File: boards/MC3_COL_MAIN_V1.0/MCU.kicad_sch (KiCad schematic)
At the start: 19 parts, among them J2 SWD, SW1 SKRKAEE020, U2 STM32F411RET6, Y1 8MHz

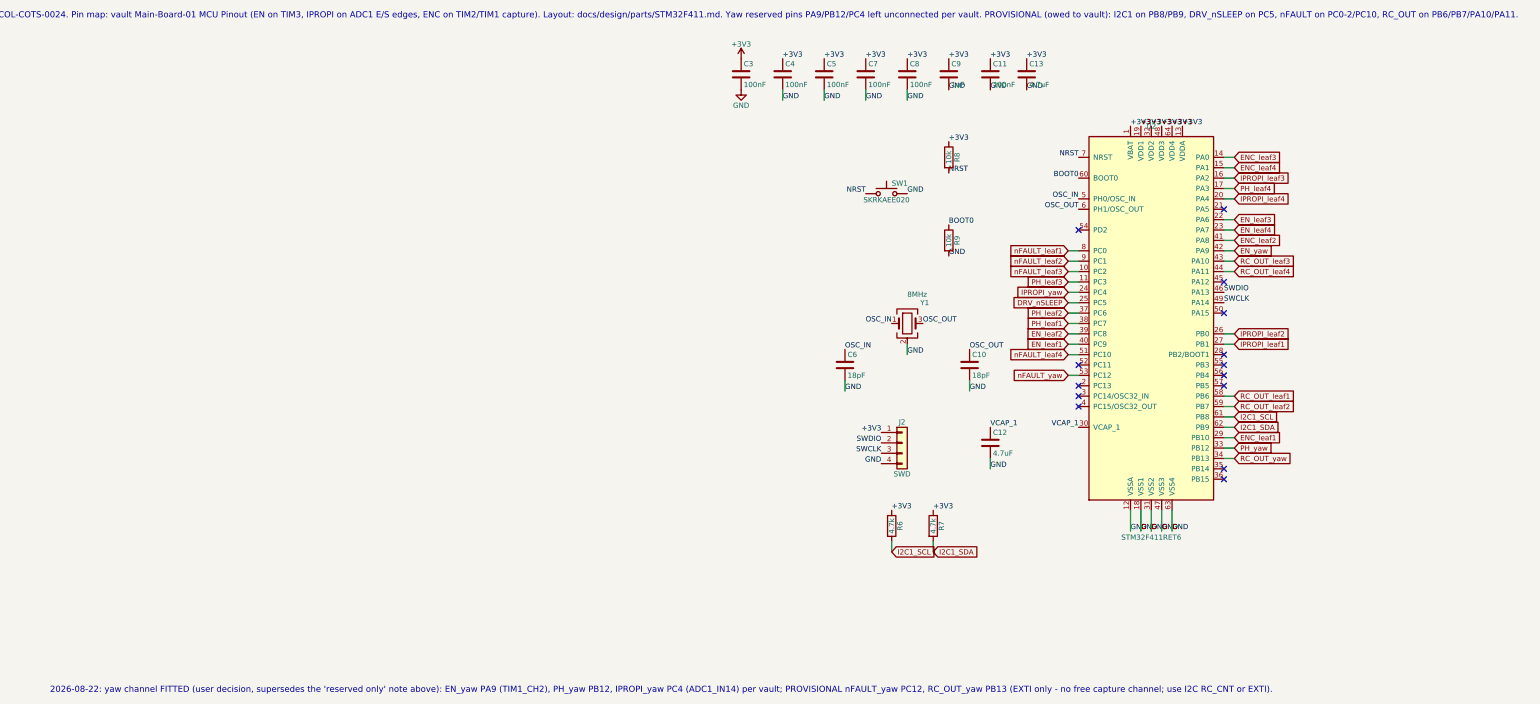
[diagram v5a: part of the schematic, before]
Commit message: Design review changes: HSE caps 33pF, R_IPROPI 6.8k (1.99 A trip), VM bulk, sensor rail filter, input fuse+TVS, NRST cap, 6-pin SWD with SWO, VDDA ferrite, LEDs, test points, tantalum LDO cap
- MCU: C6/C10 18pF -> 33pF (X32258MSB4SI is CL=20pF); C60 100nF on NRST; J2 -> Conn_01x06
  (+NRST, +SWO on PB3); VDDA split from +3V3 through FB60 + PWR_FLAG; heartbeat LED D60/R60
  on PA5, power LED D61/R61; test points TP60-64 (+3V3, SCL, SDA, IPROPI_leaf1, GND)
- Power: J1 -> VIN_PAD -> F60 polyfuse -> VIN_PROT; D62 SMAJ5.0A TVS VIN_PROT-GND; C61/C62
  2x22uF VM bulk; TP65 VM, TP66 VIN_PROT; C2 LDO output cap -> tantalum 22uF 10V (C_Polarized,
  CP_EIA-3216-18)
- Connectors: FFC VIN now VSENS = VM through FB61 + C63 4.7uF
- MotorChannel: R_IPROPI 8.45k -> 6.8k (I_TRIP = 3.3/(6.8k*244uA/A) = 1.99 A)
- Library: stock L_0603, D_SMA, Fuse_1206, CP_EIA-3216-18, TestPoint_Pad_1.0x1.0mm, LED_0603,
  PinHeader_1x06 footprints copied in
- ERC 0 errors (same_local_global_label warnings only); netlist walked

Co-Authored-By: Claude Fable 5 <noreply@anthropic.com>
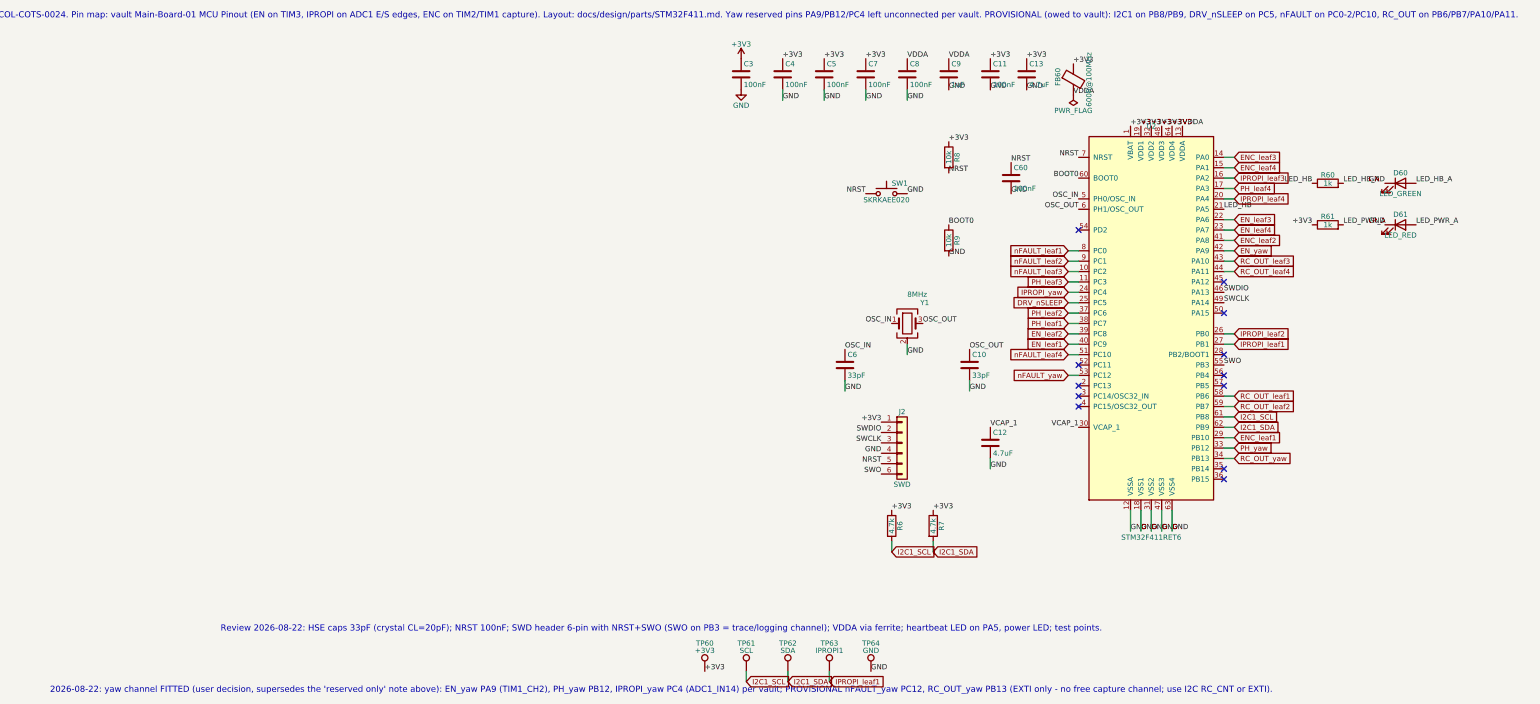
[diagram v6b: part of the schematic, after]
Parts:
- removed J2: SWD, MC3_COL_MAIN:PinHeader_1x04_P2.54mm_Vertical, symbol Connector_Generic:Conn_01x04
- added C60: 100nF, MC3_COL_MAIN:C_0402_1005Metric, symbol Device:C
- added D60: LED_GREEN, MC3_COL_MAIN:LED_0603_1608Metric, symbol Device:LED
- added D61: LED_RED, MC3_COL_MAIN:LED_0603_1608Metric, symbol Device:LED
- added FB60: 600R@100MHz, MC3_COL_MAIN:L_0603_1608Metric, symbol Device:FerriteBead
- added J2: SWD, MC3_COL_MAIN:PinHeader_1x06_P2.54mm_Vertical, symbol Connector_Generic:Conn_01x06
- added R60, R61: 1k, MC3_COL_MAIN:R_0402_1005Metric, symbol Device:R
- added TP60: +3V3, MC3_COL_MAIN:TestPoint_Pad_1.0x1.0mm, symbol Connector:TestPoint
- added TP61: SCL, MC3_COL_MAIN:TestPoint_Pad_1.0x1.0mm, symbol Connector:TestPoint
- added TP62: SDA, MC3_COL_MAIN:TestPoint_Pad_1.0x1.0mm, symbol Connector:TestPoint
- added TP63: IPROPI1, MC3_COL_MAIN:TestPoint_Pad_1.0x1.0mm, symbol Connector:TestPoint
- added TP64: GND, MC3_COL_MAIN:TestPoint_Pad_1.0x1.0mm, symbol Connector:TestPoint
- C10: value 18pF -> 33pF; Note HSE load cap 18pF -> HSE load cap 33pF (see C6)
- C6: value 18pF -> 33pF; Note HSE load cap 18pF - for X32258MSB4SI specifically -> HSE load cap 33pF: X32258MSB4SI is CL=20pF (LCSC C2682774);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
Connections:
- net +3V3: now also FB60.1, J2.1 (Pin_1), R61.1, TP60.1; no longer C8.1, C9.1, U2.13 (VDDA)
- net GND: now also C60.2, D60.1 (K), D61.1 (K), J2.4 (Pin_4), TP64.1
- net I2C1_SCL: now also TP61.1
- net I2C1_SDA: now also TP62.1
- net IPROPI_leaf1: now also TP63.1
- net NRST: now also C60.1, J2.5 (Pin_5)
- net SWCLK: now also J2.3 (Pin_3)
- net SWDIO: now also J2.2 (Pin_2)
- net LED_HB: now reaches U2.21 (PA5)
- net LED_HB: now also R60.1
- net SWO: now reaches U2.55 (PB3)
- net SWO: now also J2.6 (Pin_6)
- new net LED_HB_A: D60.2 (A), R60.2
- new net LED_PWR_A: D61.2 (A), R61.2
- new net VDDA: C8.1, C9.1, FB60.2, U2.13 (VDDA)
- no-connect marks 14 -> 12
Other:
- note added: "Review 2026-08-22: HSE caps 33pF (crystal CL=20pF); NRST 100nF; SWD header 6-pin with NRST+SWO (SWO on PB3 = trace/logging channel); VDDA via ferrite; heartbeat LED on PA5, power LED; test points."

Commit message: LCSC/MPN fields on every support part (verified against the JLCPCB DB); R_IPROPI 6.8k = C93940; polyfuse 1206L200/12NR; MIGRATION register
Co-Authored-By: Claude Fable 5 <noreply@anthropic.com>
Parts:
- C10, C6: LCSC (none) -> C1562; MPN (none) -> 0402CG330J500NT
- C11, C3, C4, C5, C60, C7, C8: LCSC (none) -> C1525; MPN (none) -> CL05B104KO5NNNC
- C12: LCSC (none) -> C19666; MPN (none) -> CL10A475KO8NNNC
- C13: LCSC (none) -> C1779; MPN (none) -> CL21A475KAQNNNE
- C9: LCSC (none) -> C52923; MPN (none) -> CL05A105KA5NQNC
- D60: LCSC (none) -> C12624; MPN (none) -> KT-0603G
- D61: LCSC (none) -> C2286; MPN (none) -> KT-0603R
- FB60: LCSC (none) -> C1002; MPN (none) -> GZ1608D601TF
- R6, R7: LCSC (none) -> C25900; MPN (none) -> 0402WGF4701TCE
- R60, R61: LCSC (none) -> C11702; MPN (none) -> 0402WGF1001TCE
- R8, R9: LCSC (none) -> C25744; MPN (none) -> 0402WGF1002TCE

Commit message: MCU -> STM32F412RET6 (pin-identical, adds bxCAN); CAN sheet: TJA1051T/3, split termination + jumper, PESD1CAN, CANH/CANL/GND pads
- MCU: U2 symbol MC3_COL_MAIN:STM32F412RET6 (same pin map as the F411), LCSC C89374; CAN1_RX PA11,
  CAN1_TX PA12; RC_OUT_leaf4 moved PA11 -> PB14
- CAN.kicad_sch (root sheet 'CAN'): U70 TJA1051T/3 (C38695) VCC from VM via FB62 + C70/C71,
  VIO +3V3, S low; JP70 solder jumper (bridged) -> R70/R71 62R split termination with C72 4.7nF;
  D70 PESD1CAN (C15771); J70 3 bare pads CANH/CANL/GND (new footprint SolderPads_3x)
- Library: STM32F412RET6 symbol; SolderPads_3x_2.2x1.4mm_P2.6mm, SOT-23, SolderJumper-2 footprints
- ERC 0 errors; netlist checked

Co-Authored-By: Claude Fable 5 <noreply@anthropic.com>
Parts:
- U2: value STM32F411RET6 -> STM32F412RET6; symbol MC3_COL_MAIN:STM32F411RET6 -> MC3_COL_MAIN:STM32F412RET6; COTS COL-COTS-0024 -> COL-COTS-TBD (new record: supersedes COL-COTS-0024 STM32F41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; LCSC C94355 -> C89374; MPN STM32F411RET6 -> STM32F412RET6
- renumbered C8 to C10, C9 to C11, C10 to C12, C11 to C13, C12 to C14, C60 to C15, C13 to C16, C3 to C5, C4 to C6, C5 to C7, C6 to C8, C7 to C9, D60 to D2, D61 to D3, FB60 to FB1, R60 to R10, R61 to R11, TP60 to TP3, TP61 to TP4, TP62 to TP5, TP63 to TP6, TP64 to TP7
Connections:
- net RC_OUT_leaf4: now also U2.35 (PB14); no longer U2.44 (PA11)
- net CAN1_TX: now reaches U2.45 (PA12/CAN1_TX)
- new net CAN1_RX: U2.44 (PA11/CAN1_RX)
- no-connect marks 12 -> 10
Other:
- note added: "2026-08-22: MCU is now STM32F412RET6 (pin-identical to the F411RET6; adds bxCAN x2 and 256 KB RAM). CAN1 on PA11 (RX) / PA12 (TX), AF9. RC_OUT_leaf4 moved PA11 -> PB14 (EXTI only). Vault: new COTS record for the F412 + MCU Pinout update owed."
